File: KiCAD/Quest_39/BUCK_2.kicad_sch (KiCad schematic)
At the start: 21 parts

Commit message: Fixed most ERC errors
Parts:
- gave numbers to parts that had none: 21
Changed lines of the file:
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@@
   (symbol (lib_id "Device:C") (at 337.82 224.79 0) (unit 1)
     (in_bom yes) (on_board yes) (fields_autoplaced)
-    (property "Reference" "C?" (id 0) (at 341.63 223.5199 0)
+    (property "Reference" "C52" (id 0) (at 341.63 223.5199 0)
       (effects (font (size 1.27 1.27)) (justify left))
     )
@@
   (symbol (lib_id "Device:R") (at 60.96 49.53 0) (unit 1)
     (in_bom yes) (on_board yes) (fields_autoplaced)
-    (property "Reference" "R?" (id 0) (at 63.5 48.2599 0)
+    (property "Reference" "R20" (id 0) (at 63.5 48.2599 0)
       (effects (font (size 1.27 1.27)) (justify left))
     )
@@
   (symbol (lib_id "Device:C_Polarized") (at 368.3 172.72 0) (unit 1)
     (in_bom yes) (on_board yes)
-    (property "Reference" "C?" (id 0) (at 372.0895 171.4075 0)
+    (property "Reference" "C49" (id 0) (at 372.0895 171.4075 0)
       (effects (font (size 1.27 1.27)) (justify left))
     )
@@
   (symbol (lib_id "Device:C") (at 128.27 137.16 0) (unit 1)
     (in_bom yes) (on_board yes) (fields_autoplaced)
-    (property "Reference" "C?" (id 0) (at 132.08 135.8899 0)
+    (property "Reference" "C46" (id 0) (at 132.08 135.8899 0)
       (effects (font (size 1.27 1.27)) (justify left))
     )
@@
   (symbol (lib_id "Device:C_Polarized") (at 354.33 172.72 0) (unit 1)
     (in_bom yes) (on_board yes)
-    (property "Reference" "C?" (id 0) (at 358.1195 171.4075 0)
+    (property "Reference" "C48" (id 0) (at 358.1195 171.4075 0)
       (effects (font (size 1.27 1.27)) (justify left))
     )
@@
   (symbol (lib_id "Device:C") (at 55.88 55.88 90) (unit 1)
     (in_bom yes) (on_board yes)
-    (property "Reference" "C?" (id 0) (at 55.88 52.07 90))
+    (property "Reference" "C45" (id 0) (at 55.88 52.07 90))
     (property "Value" "1uF" (id 1) (at 55.88 59.69 90))
     (property "Footprint" "OptoDevice:R_LDR_4.9x4.2mm_P2.54mm_Vertical" (id 2) (at 59.69 54.9148 0)
@@
   (symbol (lib_id "Device:R") (at 127 91.44 0) (unit 1)
     (in_bom yes) (on_board yes) (fields_autoplaced)
-    (property "Reference" "R?" (id 0) (at 129.54 90.1699 0)
+    (property "Reference" "R21" (id 0) (at 129.54 90.1699 0)
       (effects (font (size 1.27 1.27)) (justify left))
     )
@@
   (symbol (lib_id "Device:C") (at 125.73 46.99 0) (unit 1)
     (in_bom yes) (on_board yes) (fields_autoplaced)
-    (property "Reference" "C?" (id 0) (at 129.54 45.7199 0)
+    (property "Reference" "C44" (id 0) (at 129.54 45.7199 0)
       (effects (font (size 1.27 1.27)) (justify left))
     )
@@
   (symbol (lib_id "Analog_ADC:INA226") (at 78.74 73.66 0) (unit 1)
     (in_bom yes) (on_board yes)
-    (property "Reference" "U?" (id 0) (at 83.82 62.23 0)
+    (property "Reference" "U13" (id 0) (at 83.82 62.23 0)
       (effects (font (size 1.27 1.27)) (justify left))
     )
@@
   (symbol (lib_id "Device:R") (at 48.26 49.53 0) (unit 1)
     (in_bom yes) (on_board yes) (fields_autoplaced)
-    (property "Reference" "R?" (id 0) (at 50.8 48.2599 0)
+    (property "Reference" "R19" (id 0) (at 50.8 48.2599 0)
       (effects (font (size 1.27 1.27)) (justify left))
     )
@@
   (symbol (lib_id "Device:C_Polarized") (at 86.36 46.99 0) (unit 1)
     (in_bom yes) (on_board yes) (fields_autoplaced)
-    (property "Reference" "C?" (id 0) (at 90.17 44.8309 0)
+    (property "Reference" "C41" (id 0) (at 90.17 44.8309 0)
       (effects (font (size 1.27 1.27)) (justify left))
     )
@@
   (symbol (lib_id "Amplifier_Operational:MCP601-xOT") (at 35.56 66.04 0) (unit 1)
     (in_bom yes) (on_board yes)
-    (property "Reference" "U?" (id 0) (at 38.1 62.23 0))
+    (property "Reference" "U12" (id 0) (at 38.1 62.23 0))
     (property "Value" "MCP601T-I/OT" (id 1) (at 41.91 69.85 0))
     (property "Footprint" "Package_TO_SOT_SMD:SOT-23-5" (id 2) (at 33.02 71.12 0)
@@
   (symbol (lib_id "Device:C") (at 335.28 172.72 0) (unit 1)
     (in_bom yes) (on_board yes) (fields_autoplaced)
-    (property "Reference" "C?" (id 0) (at 339.09 171.4499 0)
+    (property "Reference" "C47" (id 0) (at 339.09 171.4499 0)
       (effects (font (size 1.27 1.27)) (justify left))
     )
@@
   (symbol (lib_id "Device:C_Polarized") (at 393.7 172.72 0) (unit 1)
     (in_bom yes) (on_board yes)
-    (property "Reference" "C?" (id 0) (at 397.4895 171.4075 0)
+    (property "Reference" "C51" (id 0) (at 397.4895 171.4075 0)
       (effects (font (size 1.27 1.27)) (justify left))
     )
@@
   (symbol (lib_id "Device:C") (at 113.03 46.99 0) (unit 1)
     (in_bom yes) (on_board yes) (fields_autoplaced)
-    (property "Reference" "C?" (id 0) (at 116.84 45.7199 0)
+    (property "Reference" "C43" (id 0) (at 116.84 45.7199 0)
       (effects (font (size 1.27 1.27)) (justify left))
     )
@@
   (symbol (lib_id "Device:R") (at 55.88 41.91 90) (unit 1)
     (in_bom yes) (on_board yes) (fields_autoplaced)
-    (property "Reference" "R?" (id 0) (at 55.88 35.56 90))
+    (property "Reference" "R18" (id 0) (at 55.88 35.56 90))
     (property "Value" "0R0025" (id 1) (at 55.88 38.1 90))
     (property "Footprint" "" (id 2) (at 55.88 43.688 90)
@@
   (symbol (lib_id "MCP4151:MCP4151-502E{slash}SN") (at 254 220.98 0) (unit 1)
     (in_bom yes) (on_board yes)
-    (property "Reference" "U?" (id 0) (at 312.42 214.63 0)
+    (property "Reference" "U15" (id 0) (at 312.42 214.63 0)
       (effects (font (size 1.524 1.524)))
     )
@@
   (symbol (lib_id "Device:C_Polarized") (at 381 172.72 0) (unit 1)
     (in_bom yes) (on_board yes)
-    (property "Reference" "C?" (id 0) (at 384.7895 171.4075 0)
+    (property "Reference" "C50" (id 0) (at 384.7895 171.4075 0)
       (effects (font (size 1.27 1.27)) (justify left))
     )
@@
   (symbol (lib_id "Device:R") (at 322.58 215.9 0) (unit 1)
     (in_bom yes) (on_board yes) (fields_autoplaced)
-    (property "Reference" "R?" (id 0) (at 325.12 214.6299 0)
+    (property "Reference" "R22" (id 0) (at 325.12 214.6299 0)
       (effects (font (size 1.27 1.27)) (justify left))
     )
@@
   (symbol (lib_id "LTM4611EV:LTM4611EV-PBF") (at 132.08 102.87 0) (unit 1)
     (in_bom yes) (on_board yes)
-    (property "Reference" "U?" (id 0) (at 308.61 50.8 0)
+    (property "Reference" "U14" (id 0) (at 308.61 50.8 0)
       (effects (font (size 1.524 1.524)))
     )
@@
   (symbol (lib_id "Device:C") (at 100.33 46.99 0) (unit 1)
     (in_bom yes) (on_board yes) (fields_autoplaced)
-    (property "Reference" "C?" (id 0) (at 104.14 45.7199 0)
-      (effects (font (size 1.27 1.27)) (justify left))
-    )
+    (property "Reference" "C42" (id 0) (at 104.14 45.7199 0)
+      (effects (font (size 1.27 1.27)) (justify left))
+    )

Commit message: Gave all INA226's unique addresses
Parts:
- removed C41: 330uF, symbol Device:C_Polarized
- removed C42: 22uF, symbol Device:C
- removed C48, C49: 100uF, symbol Device:C_Polarized
- removed C52: 100nF, symbol Device:C
- removed R18: 0R0025, symbol Device:R
- removed R19, R20: 10, symbol Device:R
- removed R21: 10K, symbol Device:R
- removed R22: 20K, symbol Device:R
- removed U12: MCP601T-I/OT, Package_TO_SOT_SMD:SOT-23-5, symbol Amplifier_Operational:MCP601-xOT
- added C42: 330uF, symbol Device:C_Polarized
- added C48, C55: 100nF, symbol Device:C
- added C49: 10nF, symbol Device:C
- added C52, C53: 100uF, symbol Device:C_Polarized
- added C54: 100pF, symbol Device:C
- added R31: 0R0025, symbol Device:R
- added R32, R33: 10R, symbol Device:R
- added R34: 9k, symbol Device:R
- added R35: 1k, symbol Device:R
- added R36: 10k, symbol Device:R
- added R37: 20K, symbol Device:R
- added TP20, TP21, TP22, TP23, TP24, TP25, TP26: TestPoint, symbol Connector:TestPoint
- added U12: AD626ANZ, N_8_ADI, symbol AD626ANZ:AD626ANZ
- C45: value 1uF -> 22uF; footprint OptoDevice:R_LDR_4.9x4.2mm_P2.54mm_Vertical -> (none)
- C46: value 100nF -> 1uF; footprint (none) -> OptoDevice:R_LDR_4.9x4.2mm_P2.54mm_Vertical
- C47: value 100pF -> 100nF
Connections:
- net +5V: now also C48.1, C55.1, U12.6 (+VS)
- net GND: now also C47.2, C48.2, C55.2, U12.2 (AGND), U12.3 (-VS); no longer U13.2 (A0), U13.3 (~{Alert})
- net NEG: now also C45.2, C42.2, C49.1, C52.2, C53.2, R35.2, U12.1 (-IN); no longer C46.2, U13.8 (Vbus)
- net P0A: now also R37.2
- net POS: now also C52.1, C53.1, C54.1; no longer C47.1
- net PV_POS: now also C43.1, C44.1, C45.1, U14.A1 (VIN), U14.A2 (VIN), U14.A3 (VIN), U14.A4 (VIN), U14.A5 (VIN), U14.A6 (VIN), U14.B1 (VIN), U14.B2 (VIN), U14.B3 (VIN), U14.B4 (VIN), U14.B5 (VIN), U14.B6 (VIN), U14.C1 (VIN), U14.C2 (VIN), U14.C3 (VIN), U14.C4 (VIN), U14.C5 (VIN), U14.C6 (VIN), C42.1, R31.1, R31.2, R32.1, R33.1, R34.1, R36.1
- net RUN: now also R36.2
- net SDA: now also U13.2 (A0)
- net TRACK/SS: now also C49.2; no longer C46.1
- net Vfb: now also C54.2, R37.1; no longer C47.2
- net Vin+: now also C46.1, R32.2; no longer C45.1
- net Vin-: now also C46.2, U13.8 (Vbus), U13.9 (Vin-), R33.2, TP21.1, U12.5 (OUT)
- net at U14.A11 (COMP): now also TP24.1
- net at U14.A7 (INTVCC): now also U14.D9 (INTVCC), TP20.1
- net at U14.B12 (PLLFLTR/FSET): now also TP23.1
- net at U14.F11 (PGOOD): now also U14.G12 (PGOOD), TP22.1
- net at U14.K12 (DIFFVOUT), U14.L12 (VOUT_LCL): now also TP25.1, TP26.1
- new net: C47.1, U12.4 (FILTER)
- new net +IN: R34.2, R35.1, U12.8 (+IN)
- no-connect marks 16 -> 12
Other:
- note added: "10:1 divider"
- note added: "Addr=0x42"
- note added: "Extra mounting"
- note added: "G=10"
- note added: "Output voltage is set by varying Rfb with a digipot. SPI = 00"
- note added: "the measured voltage is divided and then amplified by 10 as to simulate a follower. This is done to make use of the AD626 (low price and availability)."

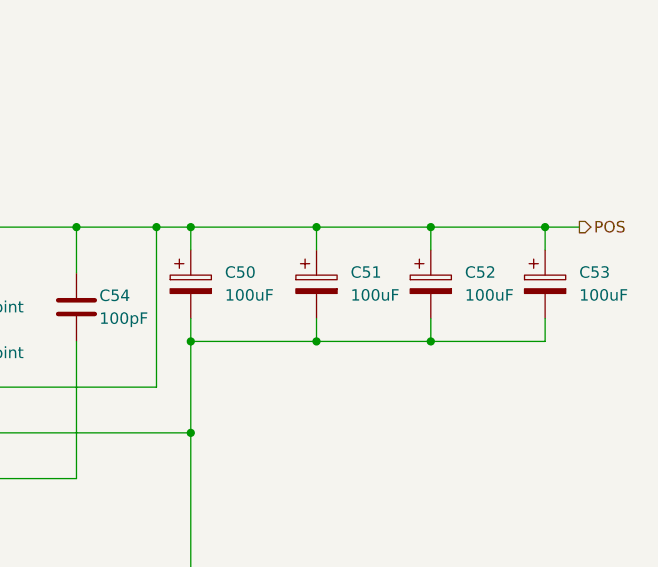
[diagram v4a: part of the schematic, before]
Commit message: Assigned all schem. symbols their footprints
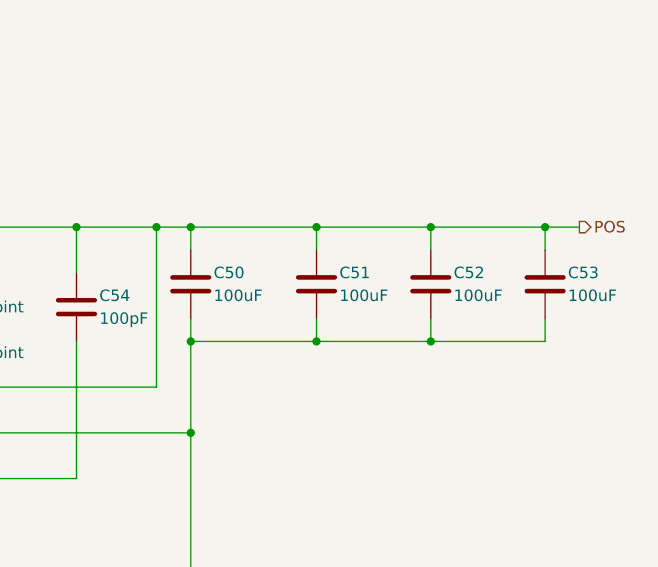
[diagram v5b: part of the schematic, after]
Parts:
- removed C50, C51, C52, C53: 100uF, symbol Device:C_Polarized
- added C50, C51, C52, C53: 100uF, Capacitor_SMD:C_1206_3216Metric, symbol Device:C
- C42: footprint (none) -> Capacitor_SMD:CP_Elec_8x6.9
- C43, C44, C45, C47, C48, C49, C54, C55: footprint (none) -> Capacitor_SMD:C_0805_2012Metric
- C46: footprint OptoDevice:R_LDR_4.9x4.2mm_P2.54mm_Vertical -> Capacitor_SMD:C_0805_2012Metric
- R31: footprint (none) -> Resistor_SMD:R_1206_3216Metric
- R32, R33, R34, R35, R36, R37: footprint (none) -> Resistor_SMD:R_0805_2012Metric
- TP20, TP21, TP22, TP23, TP24, TP25, TP26: footprint (none) -> TestPoint:TestPoint_Pad_D2.0mm
- U12: footprint N_8_ADI -> Package_DIP:DIP-8_W7.62mm_Socket_LongPads
- U14: footprint LGA-133_3_LIT -> Package_LGA:Linear_LGA-133_15.0x15.0mm_Layout12x12_P1.27mm
- U15: footprint SOIC8-N_MC_MCH -> Package_SO:MSOP-8_3x3mm_P0.65mm
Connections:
- net NEG: now also C50.2, C51.2, C52.2, C53.2
- net POS: now also C50.1, C51.1, C52.1, C53.1

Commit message: Initial work on layout
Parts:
- C46, C47, C48, C49, C54, C55: footprint Capacitor_SMD:C_0805_2012Metric -> Capacitor_SMD:C_0603_1608Metric
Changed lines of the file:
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@@
       (effects (font (size 1.27 1.27)) (justify left))
     )
-    (property "Footprint" "Capacitor_SMD:C_0805_2012Metric" (id 2) (at 341.3252 220.98 0)
+    (property "Footprint" "Capacitor_SMD:C_0603_1608Metric" (id 2) (at 341.3252 220.98 0)
       (effects (font (size 1.27 1.27)) hide)
     )
@@
       (effects (font (size 1.27 1.27)) (justify left))
     )
-    (property "Footprint" "Capacitor_SMD:C_0805_2012Metric" (id 2) (at 26.3652 81.28 0)
+    (property "Footprint" "Capacitor_SMD:C_0603_1608Metric" (id 2) (at 26.3652 81.28 0)
       (effects (font (size 1.27 1.27)) hide)
     )
@@
     (property "Reference" "C46" (id 0) (at 74.93 57.15 90))
     (property "Value" "1uF" (id 1) (at 74.93 64.77 90))
-    (property "Footprint" "Capacitor_SMD:C_0805_2012Metric" (id 2) (at 78.74 59.9948 0)
+    (property "Footprint" "Capacitor_SMD:C_0603_1608Metric" (id 2) (at 78.74 59.9948 0)
       (effects (font (size 1.27 1.27)) hide)
     )
@@
       (effects (font (size 1.27 1.27)) (justify left))
     )
-    (property "Footprint" "Capacitor_SMD:C_0805_2012Metric" (id 2) (at 64.4652 82.55 0)
+    (property "Footprint" "Capacitor_SMD:C_0603_1608Metric" (id 2) (at 64.4652 82.55 0)
       (effects (font (size 1.27 1.27)) hide)
     )
@@
       (effects (font (size 1.27 1.27)) (justify left))
     )
-    (property "Footprint" "Capacitor_SMD:C_0805_2012Metric" (id 2) (at 106.3752 124.46 0)
+    (property "Footprint" "Capacitor_SMD:C_0603_1608Metric" (id 2) (at 106.3752 124.46 0)
       (effects (font (size 1.27 1.27)) hide)
     )
@@
       (effects (font (size 1.27 1.27)) (justify left))
     )
-    (property "Footprint" "Capacitor_SMD:C_0805_2012Metric" (id 2) (at 345.1352 168.91 0)
-      (effects (font (size 1.27 1.27)) hide)
-    )
+    (property "Footprint" "Capacitor_SMD:C_0603_1608Metric" (id 2) (at 345.1352 168.91 0)
+      (effects (font (size 1.27 1.27)) hide)
+    )

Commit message: Fixed INA226 schem. mistake and further layout work
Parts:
- added C49: 100nF, Capacitor_SMD:C_0603_1608Metric, symbol Device:C
- renumbered C42 to C44, C43 to C45, C44 to C46, C45 to C47, C46 to C48, C47 to C50, C48 to C51, C49 to C52, C50 to C53, C51 to C54, C52 to C55, C53 to C56, C54 to C57, C55 to C58
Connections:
- net +5V: now also C49.1
- net GND: now also C49.2
- net PV_POS: no longer C44.1, C45.1, C46.1, C47.1, R31.2, R33.1, R36.1, U14.A1 (VIN), U14.A2 (VIN), U14.A3 (VIN), U14.A4 (VIN), U14.A5 (VIN), U14.A6 (VIN), U14.B1 (VIN), U14.B2 (VIN), U14.B3 (VIN), U14.B4 (VIN), U14.B5 (VIN), U14.B6 (VIN), U14.C1 (VIN), U14.C2 (VIN), U14.C3 (VIN), U14.C4 (VIN), U14.C5 (VIN), U14.C6 (VIN)
- net Vin-: no longer TP21.1, U12.5 (OUT), U13.8 (Vbus)
- new net: TP21.1, U12.5 (OUT), U13.8 (Vbus)
- new net BUCK_VIN: C44.1, C45.1, C46.1, C47.1, R31.2, R33.1, R36.1, U14.A1 (VIN), U14.A2 (VIN), U14.A3 (VIN), U14.A4 (VIN), U14.A5 (VIN), U14.A6 (VIN), U14.B1 (VIN), U14.B2 (VIN), U14.B3 (VIN), U14.B4 (VIN), U14.B5 (VIN), U14.B6 (VIN), U14.C1 (VIN), U14.C2 (VIN), U14.C3 (VIN), U14.C4 (VIN), U14.C5 (VIN), U14.C6 (VIN)

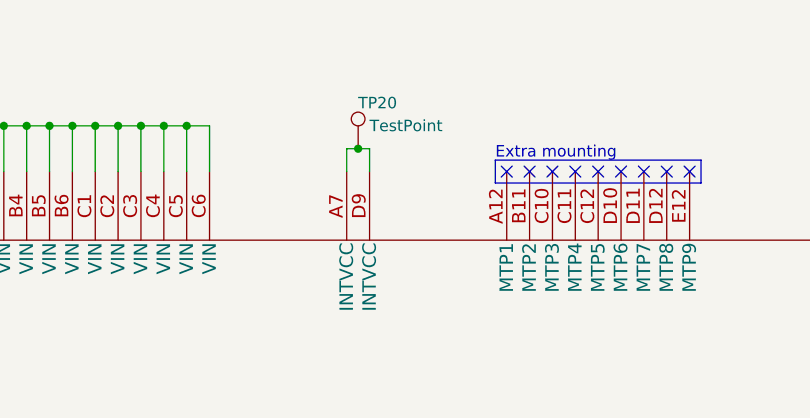
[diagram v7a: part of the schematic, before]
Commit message: Partial wiring of first buck converter section PCB layout
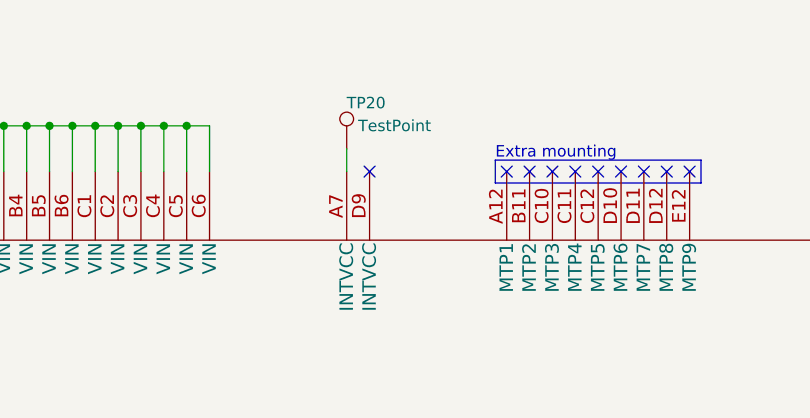
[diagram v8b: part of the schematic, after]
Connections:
- net at TP20.1, U14.A7 (INTVCC): no longer U14.D9 (INTVCC)
- no-connect marks 12 -> 13
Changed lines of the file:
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@@
   (junction (at 370.84 156.21) (diameter 0) (color 0 0 0 0)
-  )
-  (junction (at 234.95 36.83) (diameter 0) (color 0 0 0 0)
   )
   (junction (at 323.85 168.91) (diameter 0) (color 0 0 0 0)
@@
   (no_connect (at 251.46 39.37))
   (no_connect (at 271.78 39.37))
+  (no_connect (at 236.22 39.37))
   (wire (pts (xy 322.58 82.55) (xy 322.58 85.09))
     (stroke (width 0) (type default) (color 0 0 0 0))
@@
     (stroke (width 0) (type default) (color 0 0 0 0))
   )
-  (wire (pts (xy 234.95 36.83) (xy 236.22 36.83))
-    (stroke (width 0) (type default) (color 0 0 0 0))
-  )
   (wire (pts (xy 82.55 34.29) (xy 91.44 34.29))
     (stroke (width 0) (type default) (color 0 0 0 0))
@@
     (stroke (width 0) (type default) (color 0 0 0 0))
   )
-  (wire (pts (xy 236.22 36.83) (xy 236.22 39.37))
-    (stroke (width 0) (type default) (color 0 0 0 0))
-  )
   (wire (pts (xy 396.24 166.37) (xy 396.24 168.91))
     (stroke (width 0) (type default) (color 0 0 0 0))
@@
   )
   (wire (pts (xy 130.81 102.87) (xy 137.16 102.87))
-    (stroke (width 0) (type default) (color 0 0 0 0))
-  )
-  (wire (pts (xy 233.68 36.83) (xy 234.95 36.83))
     (stroke (width 0) (type default) (color 0 0 0 0))
   )
@@
     (pin "2")
   )
+  (symbol (lib_id "Connector:TestPoint") (at 233.68 36.83 0) (unit 1)
+    (in_bom yes) (on_board yes)
+    (property "Reference" "TP20" (id 0) (at 233.68 31.75 0)
+      (effects (font (size 1.27 1.27)) (justify left))
+    )
+    (property "Value" "TestPoint" (id 1) (at 234.95 34.29 0)
+      (effects (font (size 1.27 1.27)) (justify left))
+    )
+    (property "Footprint" "TestPoint:TestPoint_Pad_D2.0mm" (id 2) (at 238.76 36.83 0)
+      (effects (font (size 1.27 1.27)) hide)
+    )
+    (property "Datasheet" "~" (id 3) (at 238.76 36.83 0)
+      (effects (font (size 1.27 1.27)) hide)
+    )
+    (pin "1")
+  )
   (symbol (lib_id "AD626ANZ:AD626ANZ") (at 5.08 63.5 0) (unit 1)
     (in_bom yes) (on_board yes)
@@
     (pin "2")
   )
-  (symbol (lib_id "Connector:TestPoint") (at 234.95 36.83 0) (unit 1)
-    (in_bom yes) (on_board yes)
-    (property "Reference" "TP20" (id 0) (at 234.95 31.75 0)
-      (effects (font (size 1.27 1.27)) (justify left))
-    )
-    (property "Value" "TestPoint" (id 1) (at 236.22 34.29 0)
-      (effects (font (size 1.27 1.27)) (justify left))
-    )
-    (property "Footprint" "TestPoint:TestPoint_Pad_D2.0mm" (id 2) (at 240.03 36.83 0)
-      (effects (font (size 1.27 1.27)) hide)
-    )
-    (property "Datasheet" "~" (id 3) (at 240.03 36.83 0)
-      (effects (font (size 1.27 1.27)) hide)
-    )
-    (pin "1")
-  )
   (symbol (lib_id "Device:C") (at 105.41 120.65 0) (unit 1)
